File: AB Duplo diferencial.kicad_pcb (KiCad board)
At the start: 2 copper layers, 41 parts, among them Q1 C945, Q10 13007, Q11 13007, Q2 C945, Q3 A733, Q4 A733, Q5 A733, Q6 C945, Q7 C945, Q8 TIP41, Q9 TIP42

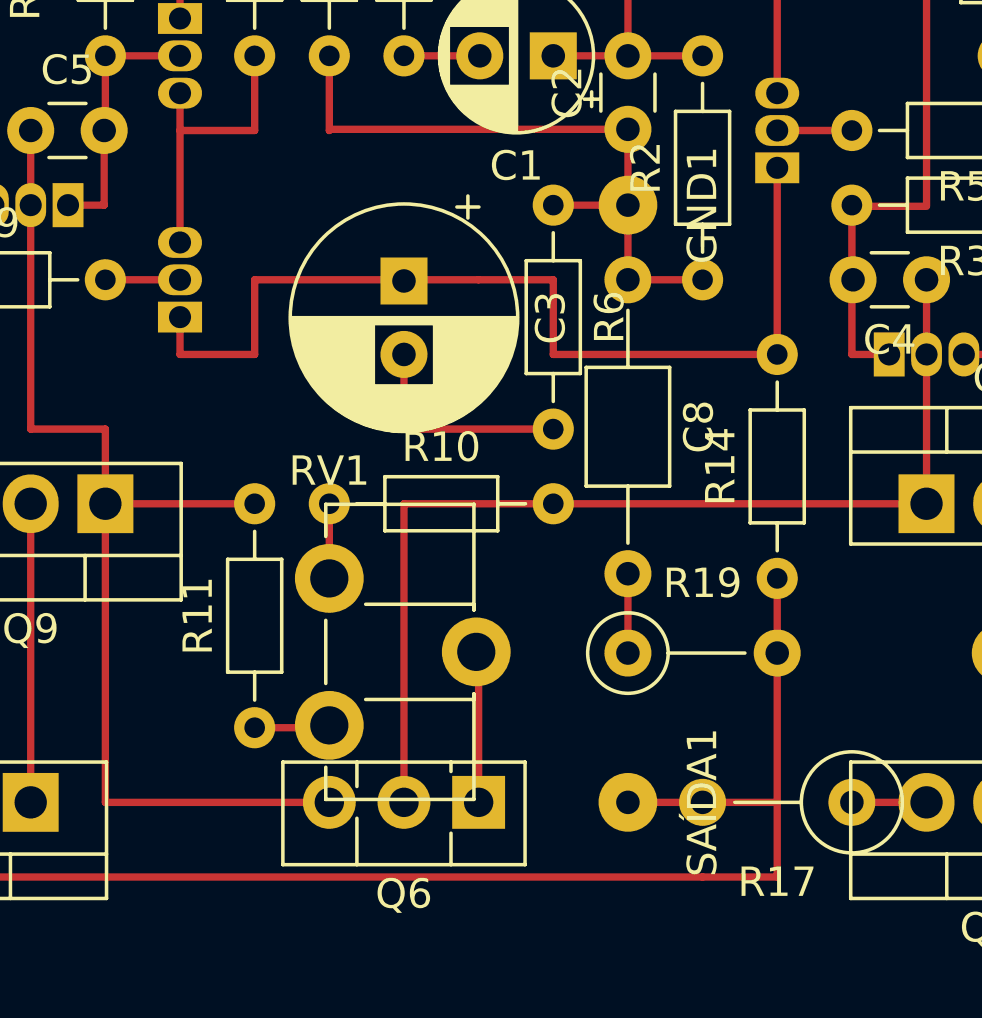
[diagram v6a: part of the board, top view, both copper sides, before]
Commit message: [rotacionados] C3 e R6 para facilitar a ligação entre Q2 e Q4
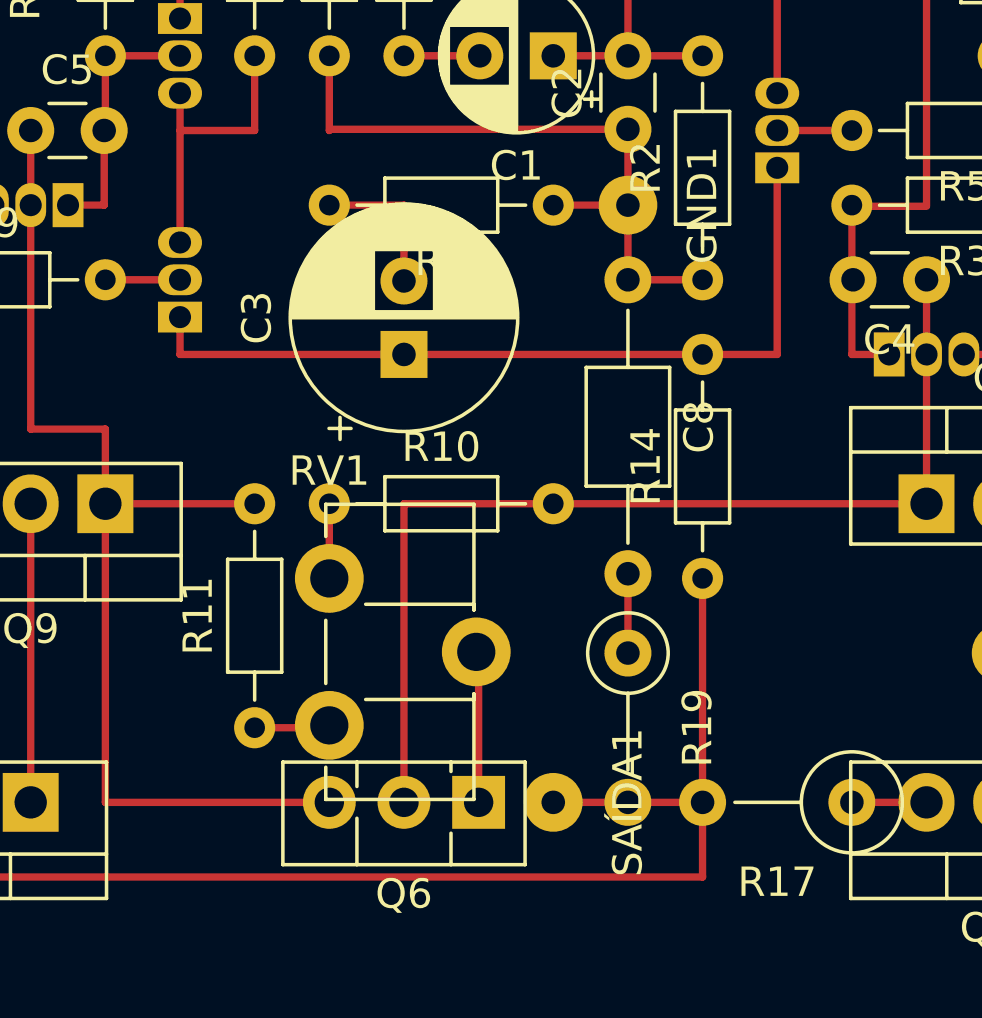
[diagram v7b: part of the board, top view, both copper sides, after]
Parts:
- moved R14 2.54 mm to (94.0, 53.3)
- moved SAÍDA1 2.54 mm to (88.9, 61.0)
- moved C3 2.50 mm to (83.8, 45.7), turned to 90 degrees
- turned R19 to 270 degrees
- turned R6 to 180 degrees
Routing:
- net Net-(C3-Pad1): track 33.0 -> 27.9 mm
- net Net-(Q11-Pad2): track 55.9 -> 53.3 mm
- net Net-(C3-Pad2): track 7.62 -> 5.12 mm
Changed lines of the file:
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@@
     (thickness 1.6)
     (drawings 0)
-    (tracks 100)
+    (tracks 91)
     (zones 0)
     (modules 41)
@@
   )
   (module Resistor_THT:R_Axial_DIN0207_L6.3mm_D2.5mm_P5.08mm_Vertical (layer F.Cu)
-    (at 91.44 55.88)
+    (at 91.44 55.88 270)
     (descr "Resistor, Axial_DIN0207 series, Axial, Vertical, pin pitch=5.08mm, 0.25W = 1/4W, length*diameter=6.3*2.5mm^2, http://cdn-reichelt.de/documents/datenblatt/B400/1_4W%23YAG.pdf")
     (tags "Resistor Axial_DIN0207 series Axial Vertical pin pitch 5.08mm 0.25W = 1/4W length 6.3mm diameter 2.5mm")
-    (fp_text reference R19 (at 2.54 -2.37) (layer F.SilkS)
-      (effects (font (size 1 1) (thickness 0.15)))
-    )
-    (fp_text value 10r (at 2.54 0) (layer F.Fab)
+    (fp_text reference R19 (at 2.54 -2.37 270) (layer F.SilkS)
+      (effects (font (size 1 1) (thickness 0.15)))
+    )
+    (fp_text value 10r (at 2.54 0 270) (layer F.Fab)
       (effects (font (size 1 1) (thickness 0.15)))
     )
@@
     (fp_line (start 6.13 1.5) (end 6.13 -1.5) (layer F.CrtYd) (width 0.05))
     (fp_line (start 6.13 -1.5) (end -1.5 -1.5) (layer F.CrtYd) (width 0.05))
-    (fp_text user %R (at 2.54 -2.37) (layer F.Fab)
-      (effects (font (size 1 1) (thickness 0.15)))
-    )
-    (pad 1 thru_hole circle (at 0 0) (size 1.6 1.6) (drill 0.8) (layers *.Cu *.Mask)
+    (fp_text user %R (at 2.54 -2.37 270) (layer F.Fab)
+      (effects (font (size 1 1) (thickness 0.15)))
+    )
+    (pad 1 thru_hole circle (at 0 0 270) (size 1.6 1.6) (drill 0.8) (layers *.Cu *.Mask)
       (net 22 "Net-(C8-Pad2)"))
-    (pad 2 thru_hole oval (at 5.08 0) (size 1.6 1.6) (drill 0.8) (layers *.Cu *.Mask)
+    (pad 2 thru_hole oval (at 5.08 0 270) (size 1.6 1.6) (drill 0.8) (layers *.Cu *.Mask)
       (net 27 "Net-(Q11-Pad2)"))
     (model ${KISYS3DMOD}/Resistor_THT.3dshapes/R_Axial_DIN0207_L6.3mm_D2.5mm_P5.08mm_Vertical.wrl
@@
   )
   (module Capacitor_THT:CP_Radial_D7.5mm_P2.50mm (layer F.Cu)
-    (at 83.82 43.22 270)
+    (at 83.82 45.72 90)
     (descr "CP, Radial series, Radial, pin pitch=2.50mm, , diameter=7.5mm, Electrolytic Capacitor")
     (tags "CP Radial series Radial pin pitch 2.50mm  diameter 7.5mm Electrolytic Capacitor")
-    (fp_text reference C3 (at 1.25 -5 270) (layer F.SilkS)
-      (effects (font (size 1 1) (thickness 0.15)))
-    )
-    (fp_text value 47uf (at -1.31 0) (layer F.Fab)
+    (fp_text reference C3 (at 1.25 -5 90) (layer F.SilkS)
+      (effects (font (size 1 1) (thickness 0.15)))
+    )
+    (fp_text value 47uf (at -1.31 0 -180) (layer F.Fab)
       (effects (font (size 1 1) (thickness 0.15)))
     )
@@
     (fp_line (start -2.892211 -2.175) (end -2.142211 -2.175) (layer F.SilkS) (width 0.12))
     (fp_line (start -2.517211 -2.55) (end -2.517211 -1.8) (layer F.SilkS) (width 0.12))
-    (fp_text user %R (at 1.25 0 270) (layer F.Fab)
-      (effects (font (size 1 1) (thickness 0.15)))
-    )
-    (pad 1 thru_hole rect (at 0 0 270) (size 1.6 1.6) (drill 0.8) (layers *.Cu *.Mask)
+    (fp_text user %R (at 1.25 0 90) (layer F.Fab)
+      (effects (font (size 1 1) (thickness 0.15)))
+    )
+    (pad 1 thru_hole rect (at 0 0 90) (size 1.6 1.6) (drill 0.8) (layers *.Cu *.Mask)
       (net 5 "Net-(C3-Pad1)"))
-    (pad 2 thru_hole circle (at 2.5 0 270) (size 1.6 1.6) (drill 0.8) (layers *.Cu *.Mask)
+    (pad 2 thru_hole circle (at 2.5 0 90) (size 1.6 1.6) (drill 0.8) (layers *.Cu *.Mask)
       (net 6 "Net-(C3-Pad2)"))
     (model ${KISYS3DMOD}/Capacitor_THT.3dshapes/CP_Radial_D7.5mm_P2.50mm.wrl
@@
   )
   (module Resistor_THT:R_Axial_DIN0204_L3.6mm_D1.6mm_P7.62mm_Horizontal (layer F.Cu)
-    (at 88.9 40.64 270)
+    (at 88.9 40.64 180)
     (descr "Resistor, Axial_DIN0204 series, Axial, Horizontal, pin pitch=7.62mm, 0.167W, length*diameter=3.6*1.6mm^2, http://cdn-reichelt.de/documents/datenblatt/B400/1_4W%23YAG.pdf")
     (tags "Resistor Axial_DIN0204 series Axial Horizontal pin pitch 7.62mm 0.167W length 3.6mm diameter 1.6mm")
-    (fp_text reference R6 (at 3.81 -1.92 270) (layer F.SilkS)
-      (effects (font (size 1 1) (thickness 0.15)))
-    )
-    (fp_text value 2k (at 3.81 0 270) (layer F.Fab)
-      (effects (font (size 1 1) (thickness 0.15)))
-    )
-    (fp_text user %R (at 3.81 0 90) (layer F.Fab)
+    (fp_text reference R6 (at 3.81 -1.92 180) (layer F.SilkS)
+      (effects (font (size 1 1) (thickness 0.15)))
+    )
+    (fp_text value 2k (at 2.01 0 180) (layer F.Fab)
+      (effects (font (size 1 1) (thickness 0.15)))
+    )
+    (fp_text user %R (at 3.81 0) (layer F.Fab)
       (effects (font (size 0.72 0.72) (thickness 0.108)))
     )
@@
     (fp_line (start 2.01 0.8) (end 5.61 0.8) (layer F.Fab) (width 0.1))
     (fp_line (start 2.01 -0.8) (end 2.01 0.8) (layer F.Fab) (width 0.1))
-    (pad 2 thru_hole oval (at 7.62 0 270) (size 1.4 1.4) (drill 0.7) (layers *.Cu *.Mask)
+    (pad 2 thru_hole oval (at 7.62 0 180) (size 1.4 1.4) (drill 0.7) (layers *.Cu *.Mask)
       (net 6 "Net-(C3-Pad2)"))
-    (pad 1 thru_hole circle (at 0 0 270) (size 1.4 1.4) (drill 0.7) (layers *.Cu *.Mask)
+    (pad 1 thru_hole circle (at 0 0 180) (size 1.4 1.4) (drill 0.7) (layers *.Cu *.Mask)
       (net 11 Earth))
     (model ${KISYS3DMOD}/Resistor_THT.3dshapes/R_Axial_DIN0204_L3.6mm_D1.6mm_P7.62mm_Horizontal.wrl
@@
   )
   (module Resistor_THT:R_Axial_DIN0204_L3.6mm_D1.6mm_P7.62mm_Horizontal (layer F.Cu)
-    (at 96.52 53.34 90)
+    (at 93.98 53.34 90)
     (descr "Resistor, Axial_DIN0204 series, Axial, Horizontal, pin pitch=7.62mm, 0.167W, length*diameter=3.6*1.6mm^2, http://cdn-reichelt.de/documents/datenblatt/B400/1_4W%23YAG.pdf")
     (tags "Resistor Axial_DIN0204 series Axial Horizontal pin pitch 7.62mm 0.167W length 3.6mm diameter 1.6mm")
@@
   )
   (module Connector_Wire:SolderWirePad_1x01_Drill0.8mm (layer F.Cu)
-    (at 91.44 60.96 270)
+    (at 88.9 60.96 270)
     (descr "Wire solder connection")
     (tags connector)
@@
   (segment (start 96.52 45.72) (end 96.52 39.37) (width 0.25) (layer F.Cu) (net 5))
   (segment (start 76.2 44.45) (end 76.2 45.72) (width 0.25) (layer F.Cu) (net 5))
-  (segment (start 76.2 45.72) (end 78.74 45.72) (width 0.25) (layer F.Cu) (net 5))
-  (segment (start 96.52 45.72) (end 88.9 45.72) (width 0.25) (layer F.Cu) (net 5))
-  (segment (start 88.9 45.72) (end 88.9 43.18) (width 0.25) (layer F.Cu) (net 5))
-  (segment (start 88.9 43.18) (end 86.36 43.18) (width 0.25) (layer F.Cu) (net 5))
-  (segment (start 78.74 45.72) (end 78.74 43.18) (width 0.25) (layer F.Cu) (net 5))
-  (segment (start 83.82 43.18) (end 78.74 43.18) (width 0.25) (layer F.Cu) (net 5))
-  (segment (start 86.36 43.18) (end 83.82 43.18) (width 0.25) (layer F.Cu) (net 5))
-  (segment (start 88.9 48.26) (end 83.82 48.26) (width 0.25) (layer F.Cu) (net 6))
-  (segment (start 83.82 48.26) (end 83.82 45.72) (width 0.25) (layer F.Cu) (net 6))
+  (segment (start 96.52 45.72) (end 76.2 45.72) (width 0.25) (layer F.Cu) (net 5))
+  (segment (start 81.28 40.64) (end 83.82 40.64) (width 0.25) (layer F.Cu) (net 6))
+  (segment (start 83.82 40.64) (end 83.82 43.22) (width 0.25) (layer F.Cu) (net 6))
   (segment (start 83.82 60.96) (end 83.82 50.8) (width 0.25) (layer F.Cu) (net 7))
   (segment (start 88.9 50.8) (end 101.6 50.8) (width 0.25) (layer F.Cu) (net 7))
@@
   (segment (start 66.04 60.96) (end 66.04 61.0075) (width 0.25) (layer F.Cu) (net 21))
   (segment (start 66.04 58.42) (end 66.04 60.96) (width 0.25) (layer F.Cu) (net 21))
-  (segment (start 91.44 55.88) (end 91.44 53.18) (width 0.25) (layer F.Cu) (net 22))
+  (segment (start 91.44 55.88) (end 91.44 53.34) (width 0.25) (layer F.Cu) (net 22))
   (segment (start 81.2 58.42) (end 81.28 58.34) (width 0.25) (layer F.Cu) (net 23))
   (segment (start 78.74 58.42) (end 81.2 58.42) (width 0.25) (layer F.Cu) (net 23))
@@
   (segment (start 86.36 27.94) (end 83.82 27.94) (width 0.25) (layer F.Cu) (net 26))
   (segment (start 83.82 27.94) (end 81.28 27.94) (width 0.25) (layer F.Cu) (net 26))
-  (segment (start 96.52 55.88) (end 96.52 53.34) (width 0.25) (layer F.Cu) (net 27))
-  (segment (start 93.98 63.5) (end 96.52 63.5) (width 0.25) (layer F.Cu) (net 27))
-  (segment (start 96.52 63.5) (end 96.52 55.88) (width 0.25) (layer F.Cu) (net 27))
-  (segment (start 93.98 60.96) (end 96.52 60.96) (width 0.25) (layer F.Cu) (net 27))
   (segment (start 68.58 50.8) (end 68.58 60.96) (width 0.25) (layer F.Cu) (net 27))
   (segment (start 68.58 60.96) (end 68.58 63.5) (width 0.25) (layer F.Cu) (net 27))
   (segment (start 68.58 63.5) (end 93.98 63.5) (width 0.25) (layer F.Cu) (net 27))
-  (segment (start 93.98 60.96) (end 91.44 60.96) (width 0.25) (layer F.Cu) (net 27))
+  (segment (start 93.98 60.96) (end 88.9 60.96) (width 0.25) (layer F.Cu) (net 27))
+  (segment (start 93.98 53.34) (end 93.98 63.5) (width 0.25) (layer F.Cu) (net 27))
 )

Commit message: [rollback] R2 & R14 pra 47k [alterado] C4 & C5 pra 47pf
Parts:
- C4, C5: value 100pf -> 47pf
- R14, R2: value 100k -> 47k
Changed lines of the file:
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@@
       (effects (font (size 1 1) (thickness 0.15)))
     )
-    (fp_text value 100pf (at 1.27 -1.27) (layer F.Fab)
+    (fp_text value 47pf (at 1.27 -1.27) (layer F.Fab)
       (effects (font (size 1 1) (thickness 0.15)))
     )
@@
       (effects (font (size 1 1) (thickness 0.15)))
     )
-    (fp_text value 100pf (at 1.25 1.27 180) (layer F.Fab)
+    (fp_text value 47pf (at 1.25 1.27 180) (layer F.Fab)
       (effects (font (size 1 1) (thickness 0.15)))
     )
@@
       (effects (font (size 1 1) (thickness 0.15)))
     )
-    (fp_text value 100k (at 3.81 0 90) (layer F.Fab)
+    (fp_text value 47k (at 3.81 0 90) (layer F.Fab)
       (effects (font (size 1 1) (thickness 0.15)))
     )
@@
       (effects (font (size 1 1) (thickness 0.15)))
     )
-    (fp_text value 100k (at 3.81 0 90) (layer F.Fab)
-      (effects (font (size 1 1) (thickness 0.15)))
-    )
+    (fp_text value 47k (at 3.81 0 90) (layer F.Fab)
+      (effects (font (size 1 1) (thickness 0.15)))
+    )
